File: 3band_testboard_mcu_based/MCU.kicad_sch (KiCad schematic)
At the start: 13 parts, among them J4 1140084168, J6 USB_C_Receptacle_USB2.0_16P, U5 ESP32-S3-WROOM-1, U7 FT232RL

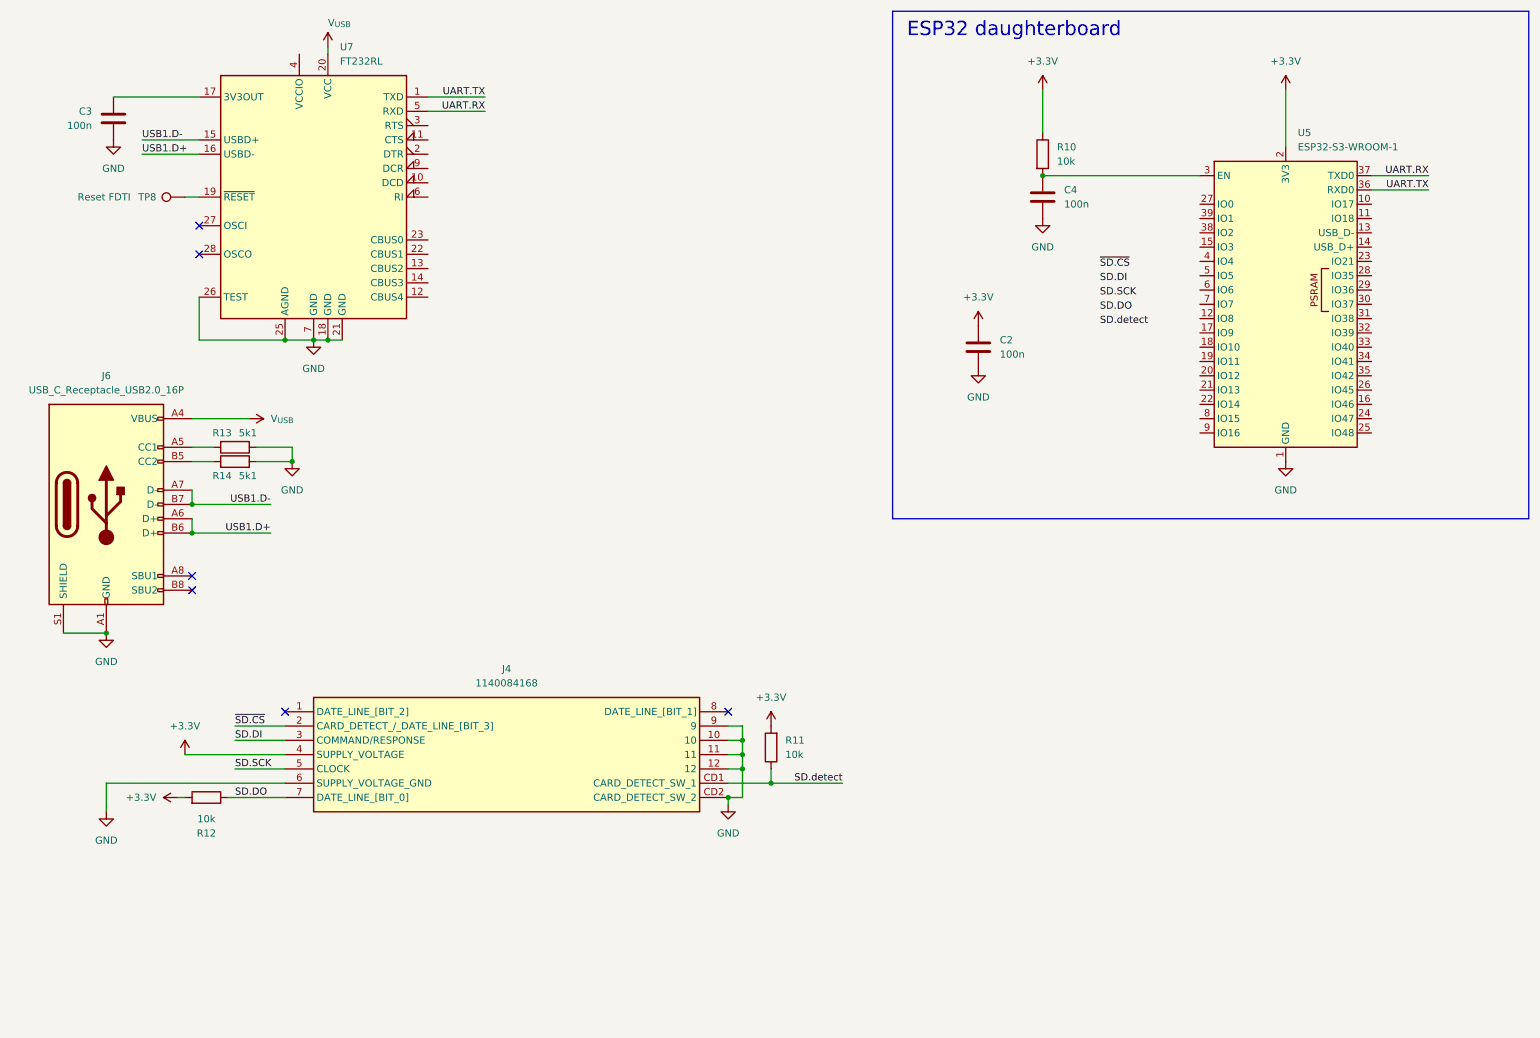
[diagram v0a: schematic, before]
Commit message: Færdiggjorde GPIO
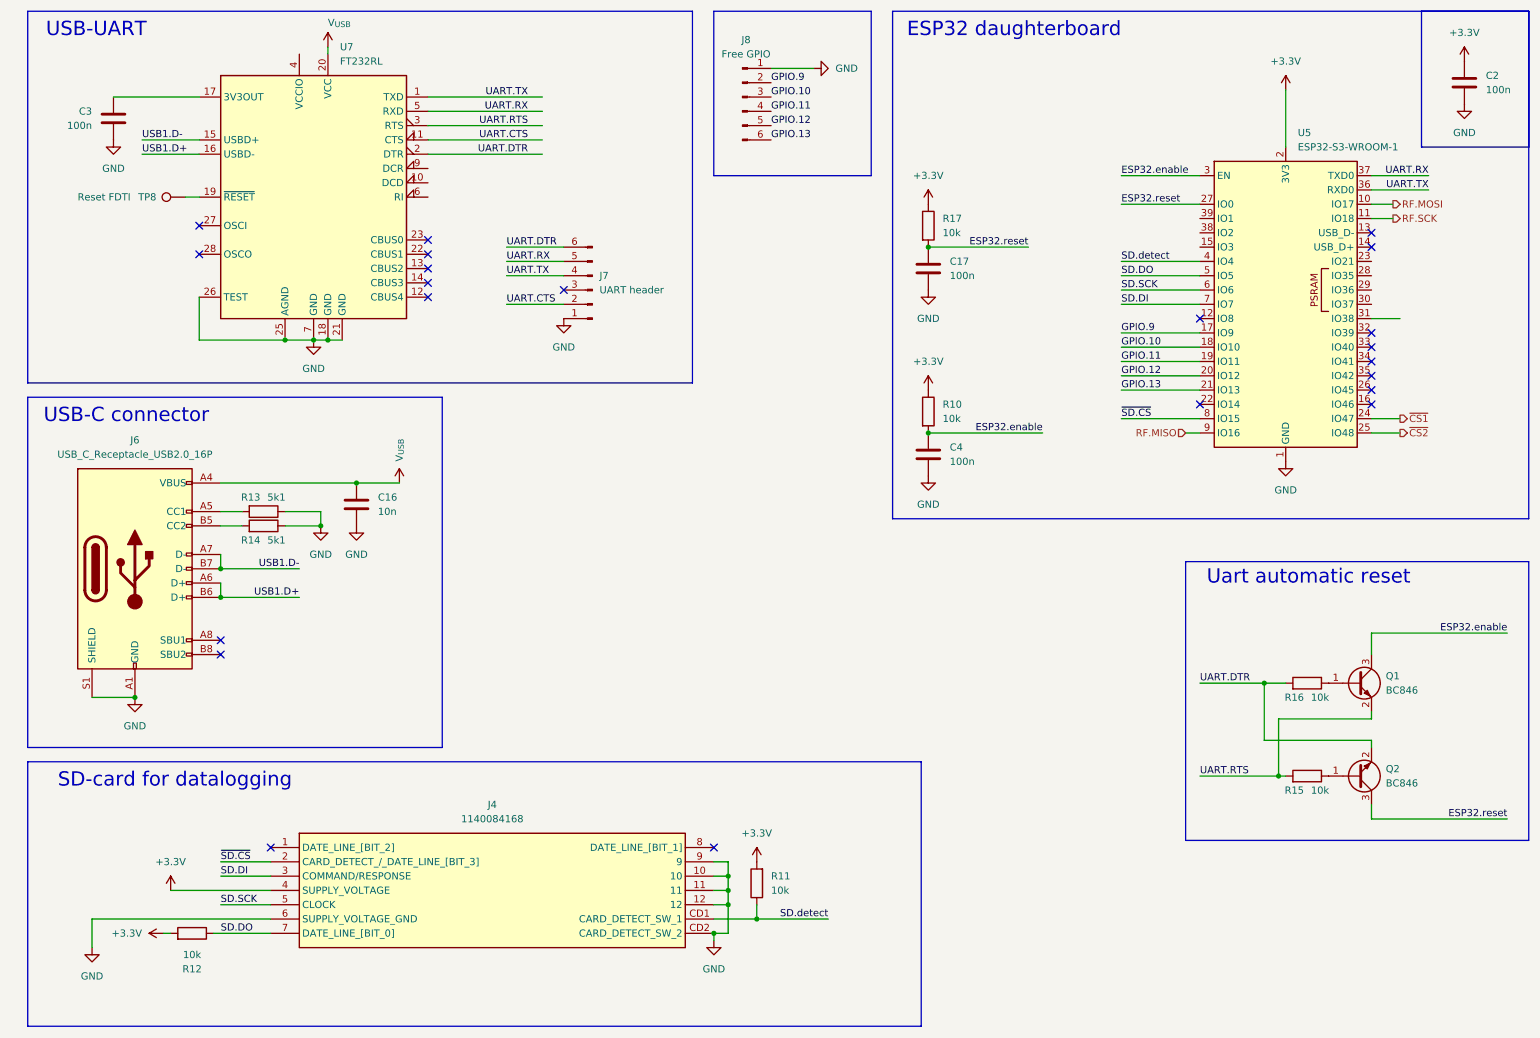
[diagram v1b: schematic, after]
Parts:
- added C16: 10n, Capacitor_SMD:C_0603_1608Metric, symbol Device:C
- added C17: 100n, Capacitor_SMD:C_0603_1608Metric, symbol Device:C
- added J7: UART header, Connector_PinSocket_2.54mm:PinSocket_1x06_P2.54mm_Vertical, symbol Connector:Conn_01x06_Pin
- added J8: Free GPIO, Connector_PinHeader_2.54mm:PinHeader_1x06_P2.54mm_Vertical, symbol Connector:Conn_01x06_Pin
- added Q1, Q2: BC846, Package_TO_SOT_SMD:SOT-23, symbol Transistor_BJT:BC846
- added R15, R16, R17: 10k, Resistor_SMD:R_0603_1608Metric, symbol Device:R
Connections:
- net +3.3V: now also R17.1
- net GND: now also C16.2, C17.2, J7.1 (Pin_1), J8.1 (Pin_1)
- net SD.DI: now also U5.7 (IO7)
- net SD.DO: now also U5.5 (IO5)
- net SD.SCK: now also U5.6 (IO6)
- net SD.detect: now also U5.4 (IO4)
- net UART.RX: now also J7.5 (Pin_5)
- net UART.TX: now also J7.4 (Pin_4)
- net V_{USB}: now also C16.1
- net ~{SD.CS}: now also U5.8 (IO15)
- net ESP32.enable: now reaches C4.1, R10.2, U5.3 (EN)
- net ESP32.enable: now also Q1.3 (C)
- net UART.CTS: now reaches U7.11 (CTS)
- net UART.CTS: now also J7.2 (Pin_2)
- net UART.DTR: now reaches U7.2 (DTR)
- net UART.DTR: now also J7.6 (Pin_6), Q2.2 (E), R16.2
- net UART.RTS: now reaches U7.3 (RTS)
- net UART.RTS: now also Q1.2 (E), R15.2
- net RF.MOSI: now reaches U5.10 (IO17)
- net RF.SCK: now reaches U5.11 (IO18)
- net GPIO.9: now reaches U5.17 (IO9)
- net GPIO.9: now also J8.2 (Pin_2)
- net GPIO.10: now reaches U5.18 (IO10)
- net GPIO.10: now also J8.3 (Pin_3)
- net GPIO.11: now reaches U5.19 (IO11)
- net GPIO.11: now also J8.4 (Pin_4)
- net GPIO.12: now reaches U5.20 (IO12)
- net GPIO.12: now also J8.5 (Pin_5)
- net GPIO.13: now reaches U5.21 (IO13)
- net GPIO.13: now also J8.6 (Pin_6)
- net ~{CS1}: now reaches U5.24 (IO47)
- net ~{CS2}: now reaches U5.25 (IO48)
- net ESP32.reset: now reaches U5.27 (IO0)
- net ESP32.reset: now also C17.1, Q2.3 (C), R17.2
- net RF.MISO: now reaches U5.9 (IO16)
- new net: Q2.1 (B), R15.1
- new net: Q1.1 (B), R16.1
- no-connect marks 6 -> 22
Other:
- note added: "SD-card for datalogging"
- note added: "USB-C connector"
- note added: "USB-UART"
- note added: "Uart automatic reset"
- company: (none) -> AAU-connectivity
- title: (none) -> 3-band-LoRa testboard
- moved on the sheet: C2, C4, J4, J6, R10, R11, R12, R13, R14

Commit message: DRC check, and price
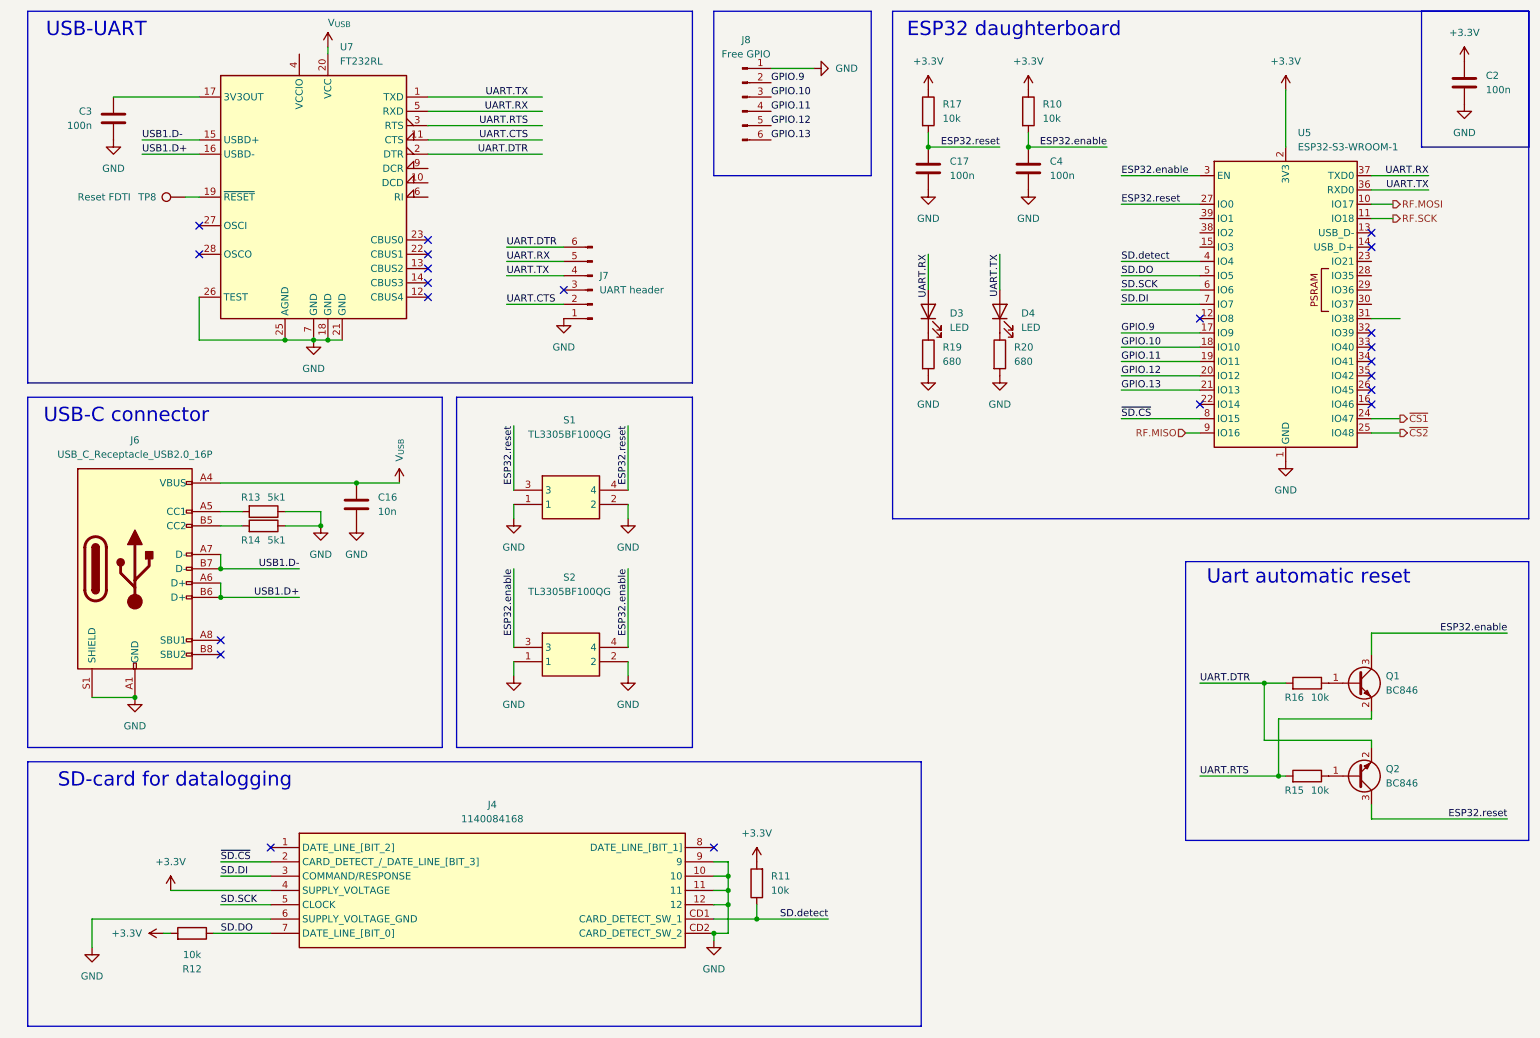
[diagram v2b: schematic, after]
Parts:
- added D3, D4: LED, LED_SMD:LED_0603_1608Metric_Pad1.05x0.95mm_HandSolder, symbol Device:LED
- added R19, R20: 680, Resistor_SMD:R_0603_1608Metric, symbol Device:R
- added S1, S2: TL3305BF100QG, TL3305BF160QG, symbol TL3305BF100QG:TL3305BF100QG
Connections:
- net ESP32.enable: now also S2.3, S2.4
- net ESP32.reset: now also S1.3, S1.4
- net GND: now also R19.2, R20.2, S1.1, S1.2, S2.1, S2.2
- net UART.RX: now also D3.2 (A)
- net UART.TX: now also D4.2 (A)
- new net: D4.1 (K), R20.1
- new net: D3.1 (K), R19.1
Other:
- moved on the sheet: C17, C4, R10, R17
